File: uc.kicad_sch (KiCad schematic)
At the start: 24 parts, among them SW2 FSMH

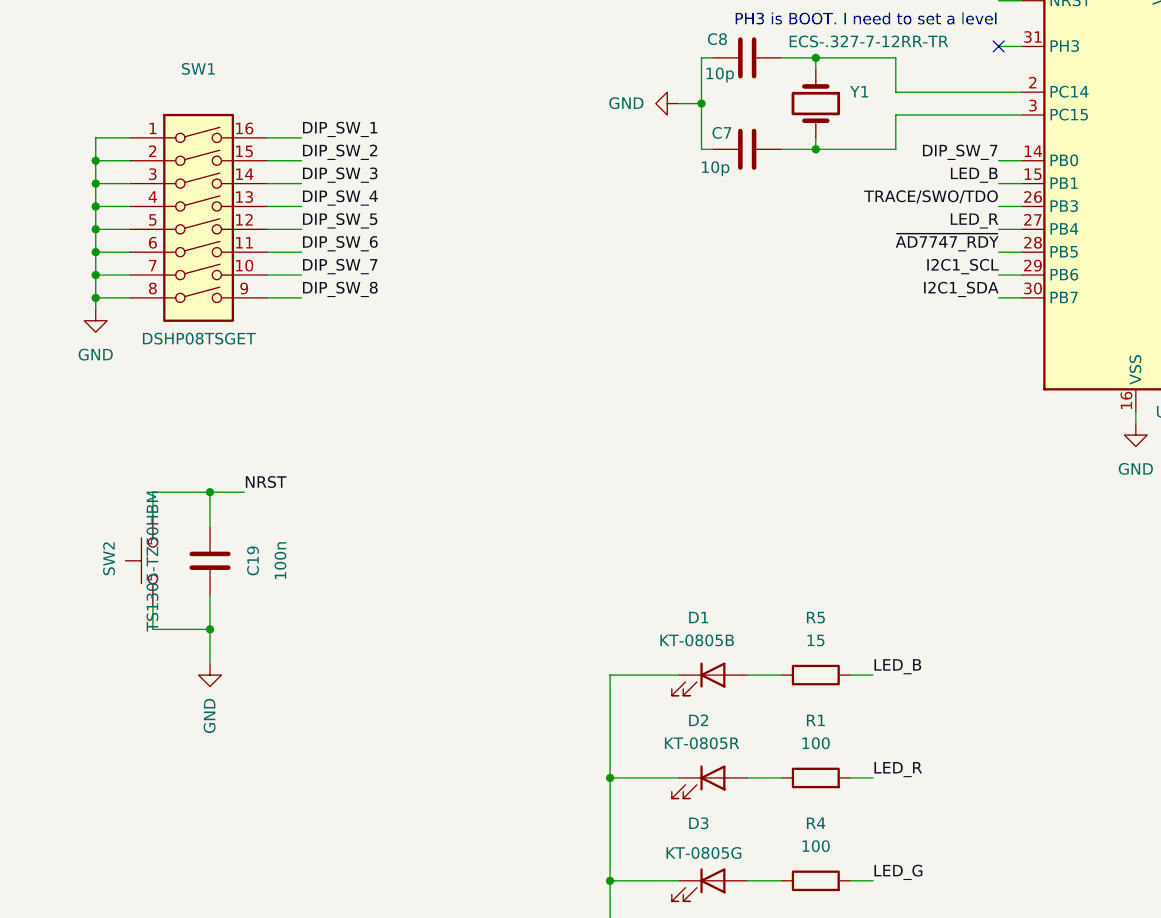
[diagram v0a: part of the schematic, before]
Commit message: bom: Optimize part selection to reduce order price at jlcpcb
- Change references to use basic components instead of 'extended components' when available
- Change button reference to use a basic component
- Change led references to use basic components
- Harmonize some resistors value to limit the number of lines in BoM
- Change transistor references for basic components
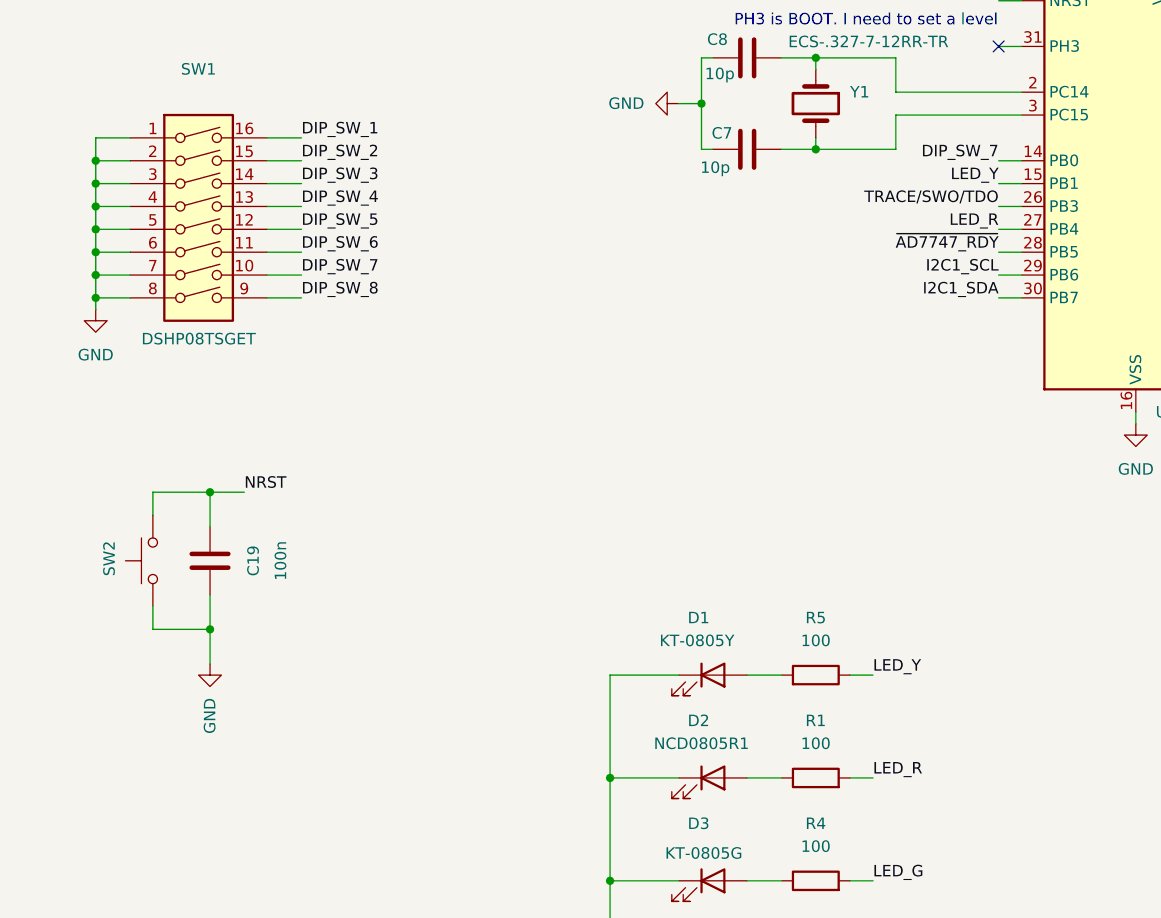
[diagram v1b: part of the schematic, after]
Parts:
- C13: LCSC C59782 -> C15849
- C7, C8: LCSC C106245 -> C1634
- D1: LCSC C2293 -> C2296; MPN KT-0805B -> KT-0805Y
- D2: LCSC C2295 -> C84256; MPN KT-0805R -> NCD0805R1
- R1, R4: LCSC C105588 -> C22775
- R2, R3: LCSC C114662 -> C4190
- R5: value 15 -> 100; LCSC C128059 -> C22775
- SW2: footprint footprints:SW_Tactile_SPST_NO_Straight_CK_PTS636Sx25SMTRLFS -> footprints:SW_Push_1P1T_XKB_TS-1187A; LCSC C36936594 -> C318884; MPN TS1305-TZ50HBM -> TS-1187A-B-A-B
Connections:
- net LED_B renamed LED_Y
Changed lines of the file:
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@@
 		)
 	)
-	(label "LED_B"
+	(label "LED_Y"
 		(at 109.22 153.67 0)
 		(effects
@@
 		)
 	)
-	(label "LED_B"
+	(label "LED_Y"
 		(at 123.19 99.06 180)
 		(effects
@@
 			)
 		)
-		(property "LCSC" "C2295"
+		(property "LCSC" "C84256"
 			(at 91.44 165.1 0)
 			(effects
@@
 			)
 		)
-		(property "MPN" "KT-0805R"
+		(property "MPN" "NCD0805R1"
 			(at 90.17 161.29 0)
 			(effects
@@
 			)
 		)
-		(property "LCSC" "C2293"
+		(property "LCSC" "C2296"
 			(at 91.44 153.67 0)
 			(effects
@@
 			)
 		)
-		(property "MPN" "KT-0805B"
+		(property "MPN" "KT-0805Y"
 			(at 89.662 149.86 0)
 			(effects
@@
 			)
 		)
-		(property "LCSC" "C106245"
+		(property "LCSC" "C1634"
 			(at 95.25 85.09 0)
 			(effects
@@
 			)
 		)
+		(property "MPN" ""
+			(at 95.25 85.09 0)
+			(effects
+				(font
+					(size 1.27 1.27)
+				)
+			)
+		)
 		(pin "2"
 		)
@@
 			)
 		)
-		(property "LCSC" "C114662"
+		(property "LCSC" "C4190"
 			(at 30.48 64.77 0)
 			(effects
@@
 			)
 		)
+		(property "MPN" ""
+			(at 30.48 64.77 0)
+			(effects
+				(font
+					(size 1.27 1.27)
+				)
+			)
+		)
 		(pin "1"
 		)
@@
 			)
 		)
-		(property "LCSC" "C105588"
+		(property "LCSC" "C22775"
 			(at 102.87 165.1 0)
 			(effects
@@
 			)
 		)
+		(property "MPN" ""
+			(at 102.87 165.1 0)
+			(effects
+				(font
+					(size 1.27 1.27)
+				)
+			)
+		)
 		(pin "1"
 		)
@@
 			)
 		)
-		(property "LCSC" "C114662"
+		(property "LCSC" "C4190"
 			(at 38.1 64.77 0)
 			(effects
@@
 			)
 		)
+		(property "MPN" ""
+			(at 38.1 64.77 0)
+			(effects
+				(font
+					(size 1.27 1.27)
+				)
+			)
+		)
 		(pin "1"
 		)
@@
 			)
 		)
-		(property "LCSC" "C106245"
+		(property "LCSC" "C1634"
 			(at 95.25 95.25 0)
 			(effects
@@
 			)
 		)
-		(property "Footprint" "footprints:SW_Tactile_SPST_NO_Straight_CK_PTS636Sx25SMTRLFS"
+		(property "Footprint" "footprints:SW_Push_1P1T_XKB_TS-1187A"
 			(at 24.13 140.97 0)
 			(effects
@@
 			)
 		)
-		(property "LCSC" "C36936594"
+		(property "LCSC" "C318884"
 			(at 29.21 140.97 0)
 			(effects
@@
 			)
 		)
-		(property "MPN" "TS1305-TZ50HBM"
-			(at 29.21 140.97 0)
+		(property "MPN" "TS-1187A-B-A-B"
+			(at 17.78 141.224 0)
 			(effects
 				(font
 					(size 1.27 1.27)
 				)
+				(hide yes)
 			)
 		)
@@
 			)
 		)
-		(property "LCSC" "C105588"
+		(property "LCSC" "C22775"
 			(at 102.87 176.53 0)
 			(effects
@@
 			)
 		)
+		(property "MPN" ""
+			(at 102.87 176.53 0)
+			(effects
+				(font
+					(size 1.27 1.27)
+				)
+			)
+		)
 		(pin "1"
 		)
@@
 			)
 		)
-		(property "Value" "15"
+		(property "Value" "100"
 			(at 102.87 149.86 90)
 			(effects
@@
 			)
 		)
-		(property "LCSC" "C128059"
+		(property "LCSC" "C22775"
 			(at 102.87 153.67 0)
 			(effects
@@
 			)
 		)
+		(property "MPN" ""
+			(at 102.87 153.67 0)
+			(effects
+				(font
+					(size 1.27 1.27)
+				)
+			)
+		)
 		(pin "1"
 		)
@@
 			)
 		)
-		(property "LCSC" "C59782"
+		(property "LCSC" "C15849"
 			(at 58.42 30.48 0)
 			(effects
@@
 			)
 		)
+		(property "MPN" ""
+			(at 58.42 30.48 0)
+			(effects
+				(font
+					(size 1.27 1.27)
+				)
+			)
+		)

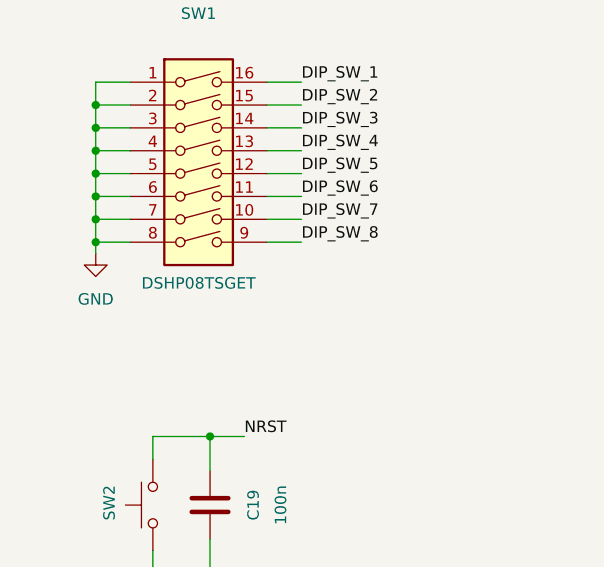
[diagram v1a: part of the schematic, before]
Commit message: bom: Fix the SW1 dip switch reference
Select a part that fit the footprint
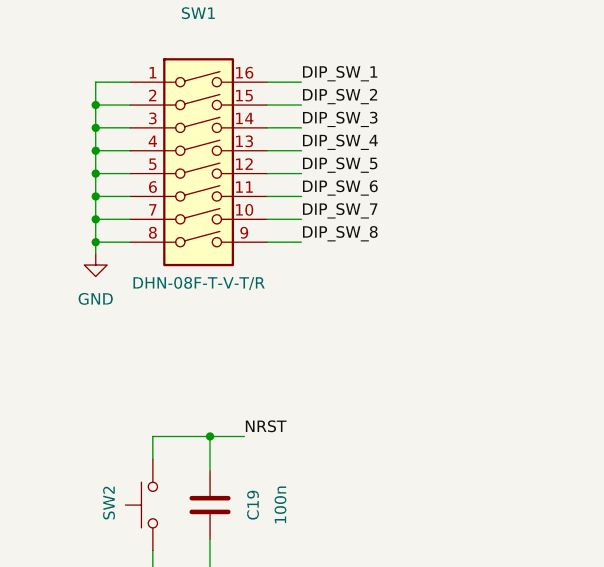
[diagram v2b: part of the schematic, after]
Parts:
- SW1: LCSC C40738 -> C89711; MPN DSHP08TSGET -> DHN-08F-T-V-T/R
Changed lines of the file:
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@@
 			)
 		)
-		(property "LCSC" "C40738"
+		(property "LCSC" "C89711"
 			(at 34.29 104.14 0)
 			(effects
@@
 			)
 		)
-		(property "MPN" "DSHP08TSGET"
+		(property "MPN" "DHN-08F-T-V-T/R"
 			(at 34.29 116.332 0)
 			(effects
